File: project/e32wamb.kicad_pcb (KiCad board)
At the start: 2 copper layers, 50 x 37 mm, 31 parts, among them J1 2059-302_998-403, J2 Conn_01x04, J3 Conn_01x03, Q1 AO3400, Q2 AO3400, Q3 AO3400, Q4 AO3400, Q5 AO3400, SW1 TS-1187A-B-A-B, U1 AP63203WU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

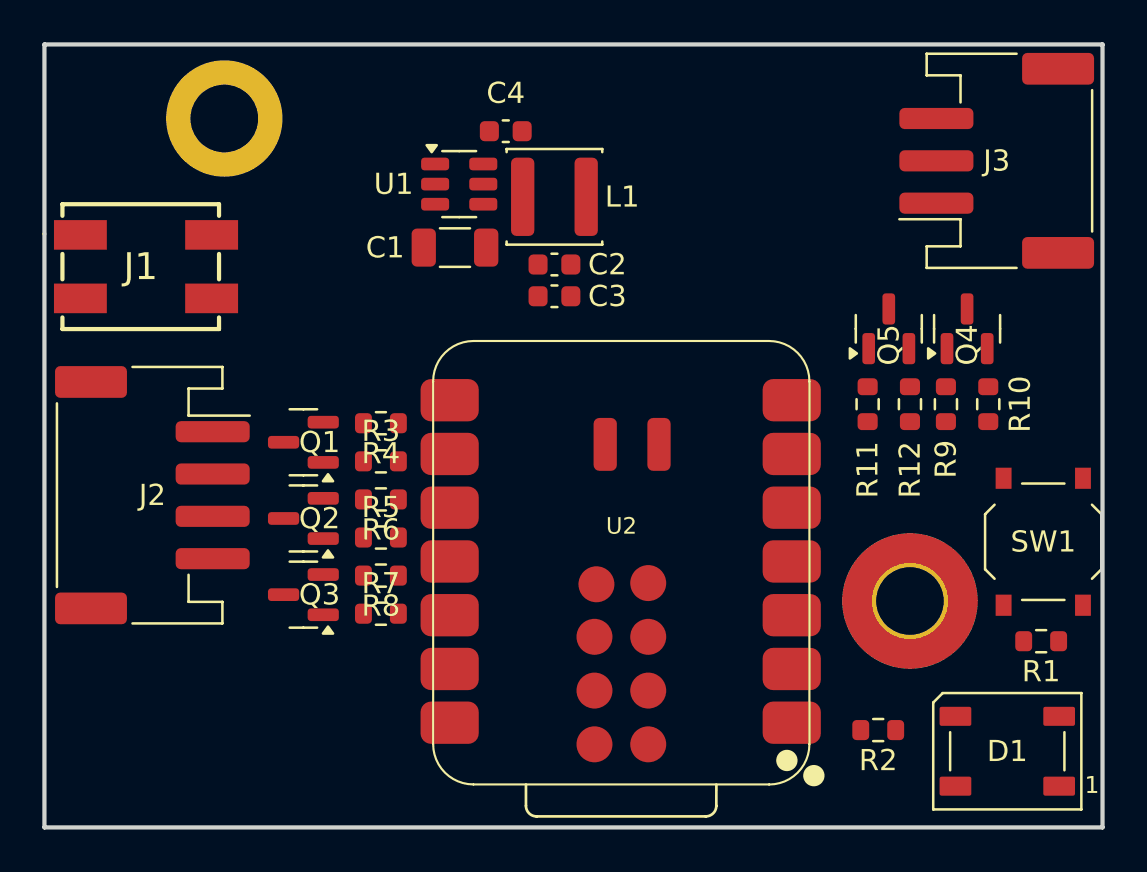
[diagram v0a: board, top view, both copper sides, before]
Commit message: First shot at wiring (complete pcb)
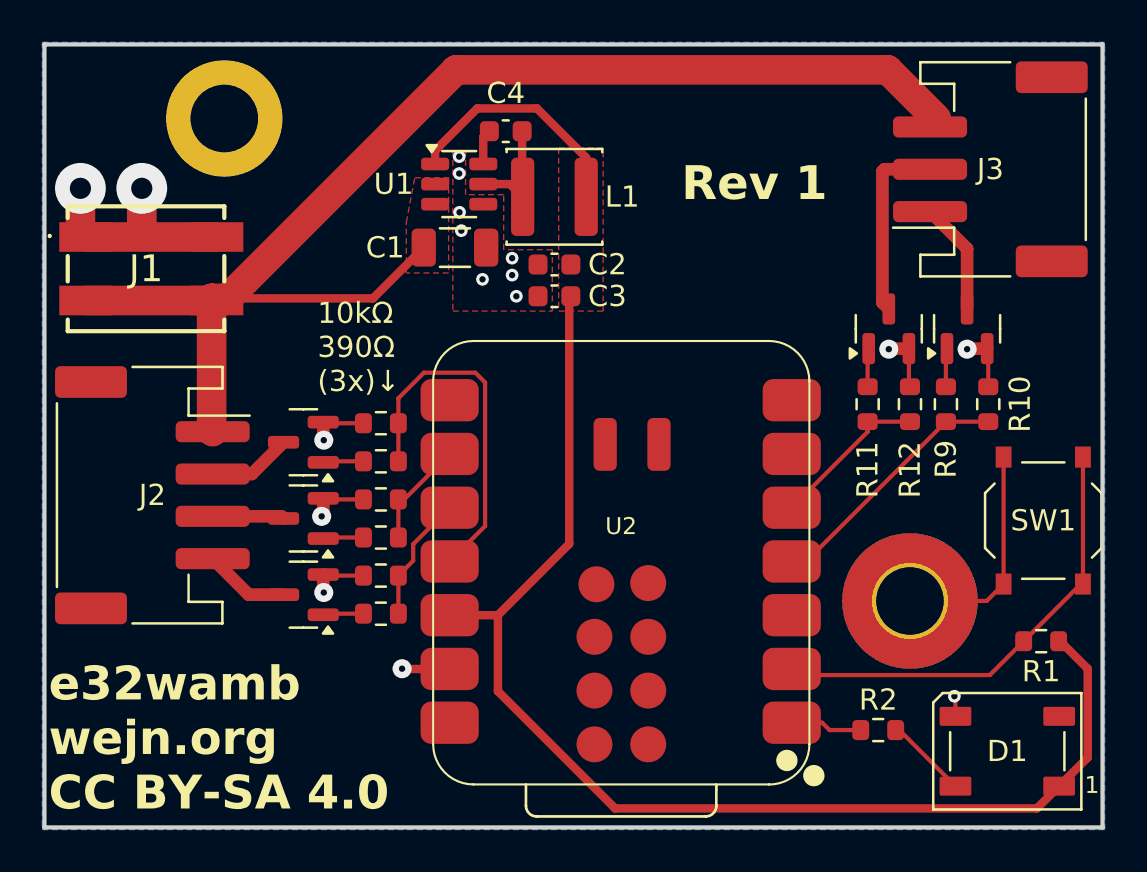
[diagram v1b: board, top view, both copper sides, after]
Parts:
- moved SW1 1.00 mm to (97.2, 72.5)
- moved J3 0.50 mm to (94.7, 55.9)
- moved J1 0.27 mm to (54.8, 60.6)
- turned R2 to 0 degrees
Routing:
- net +3.3V: track 0.00 -> 70.7 mm
- net VIN: track 0.00 -> 63.0 mm
- net GND: track 0.00 -> 39.2 mm, vias 0 -> 17
- net reset button: track 0.00 -> 21.7 mm
- net pwm drive 0: track 0.00 -> 16.9 mm
- net pwm drive 3: track 0.00 -> 12.0 mm
- net led 4: track 0.00 -> 8.92 mm
- net pwm drive 4: track 0.00 -> 7.55 mm
- net pwm drive 2: track 0.00 -> 6.01 mm
- net led 3: track 0.00 -> 5.32 mm
- net Net-(U1-SW): track 0.00 -> 5.22 mm
- net pwm drive 1: track 0.00 -> 5.11 mm
- net led 2: track 0.00 -> 4.05 mm
- net led 0: track 0.00 -> 3.97 mm
- net Net-(D1-DIN): track 0.00 -> 3.92 mm
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- added copper zone on F.Cu, net +3.3V
- added copper zone on B.Cu, net GND
- added copper zone on F.Cu, net GND
- added copper zone on F.Cu, net VIN
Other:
- board text added: "10kΩ 390Ω (3x)↓"
- board text added: "Rev 1"
- board text added: "e32wamb wejn.org CC BY-SA 4.0"

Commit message: Fix mounting hole h2 footprint
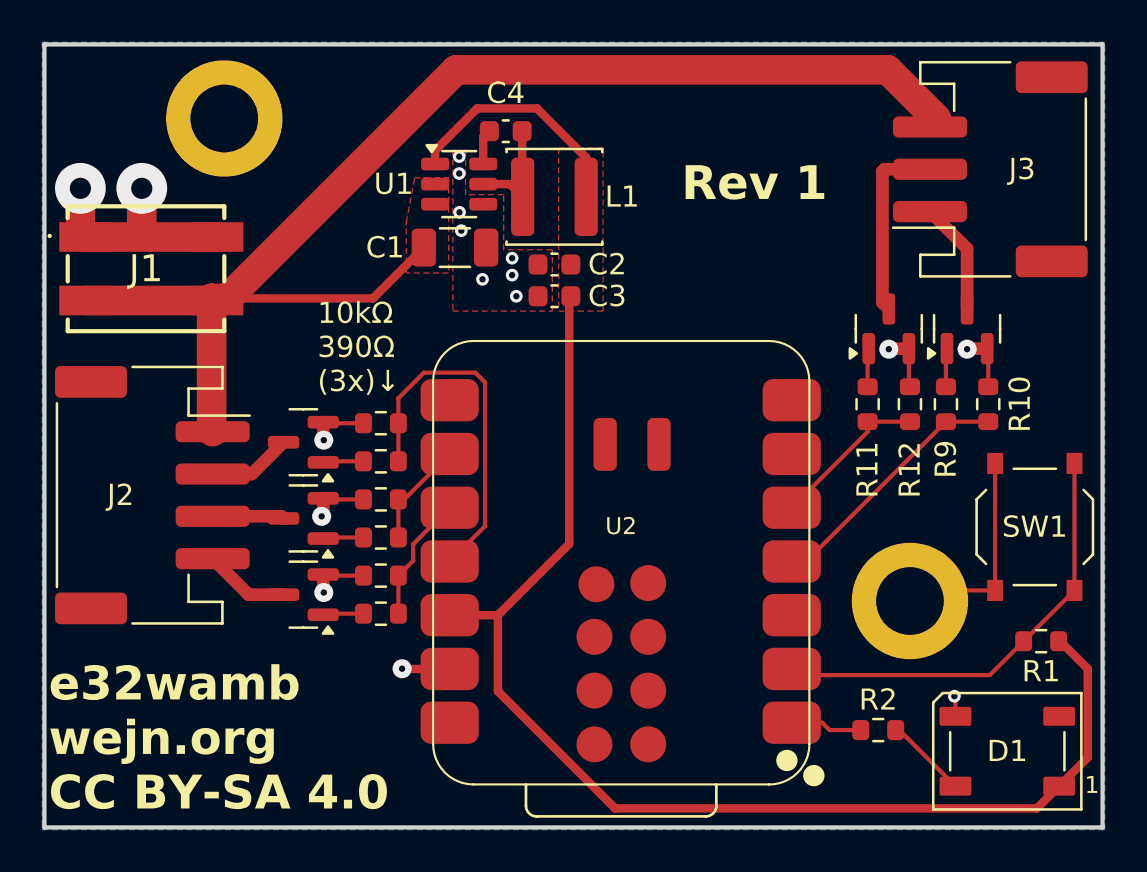
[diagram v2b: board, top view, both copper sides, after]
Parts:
- H2: footprint MountingHole:MountingHole_3.2mm_M3_Pad_TopBottom -> MountingHole:MountingHole_3.2mm_M3_ISO14580_Pad
- moved SW1 0.50 mm to (96.8, 72.8)
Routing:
- net reset button: track 21.7 -> 21.1 mm
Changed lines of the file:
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@@
 			(pdf_back_fp_property_popups yes)
 			(pdf_metadata yes)
-			(pdf_single_document no)
+			(pdf_single_document yes)
 			(dxfpolygonmode yes)
 			(dxfimperialunits yes)
@@
 			(psnegative no)
 			(psa4output no)
-			(plot_black_and_white yes)
+			(plot_black_and_white no)
 			(plotinvisibletext no)
 			(sketchpadsonfab no)
@@
 			(crossoutdnponfab yes)
 			(subtractmaskfromsilk no)
-			(outputformat 1)
+			(outputformat 4)
 			(mirror no)
-			(drillshape 1)
+			(drillshape 0)
 			(scaleselection 1)
-			(outputdirectory "")
+			(outputdirectory "/home/wejn/zz/")
 		)
 	)
@@
 		(tags "connector JST PH horizontal")
 		(property "Reference" "J2"
-			(at 0 0 0)
+			(at 0 1.5 0)
 			(layer "F.SilkS")
 			(effects
@@
 		)
 		(fp_text user "${REFERENCE}"
-			(at 0 1.5 90)
+			(at 0 1.5 180)
 			(layer "F.Fab")
 			(effects
@@
 		(tags "connector JST PH horizontal")
 		(property "Reference" "J3"
-			(at 0 0 180)
+			(at 0 1.5 180)
 			(layer "F.SilkS")
 			(effects
@@
 		)
 		(fp_text user "${REFERENCE}"
-			(at 0 1.5 90)
+			(at 0 1.5 180)
 			(layer "F.Fab")
 			(effects
@@
 		)
 	)
-	(footprint "MountingHole:MountingHole_3.2mm_M3_Pad_TopBottom"
+	(footprint "MountingHole:MountingHole_3.2mm_M3_ISO14580_Pad"
 		(layer "F.Cu")
 		(at 90.9 76.3)
-		(descr "Mounting Hole 3.2mm, M3")
-		(tags "mounting hole 3.2mm m3")
+		(descr "Mounting Hole 3.2mm, M3, ISO14580")
+		(tags "mounting hole 3.2mm m3 iso14580")
 		(property "Reference" "H2"
-			(at 0 -4.2 0)
+			(at 0 -3.75 0)
 			(layer "F.SilkS")
 			(hide yes)
@@
 		)
 		(property "Value" "MountingHole_Pad"
-			(at 0 4.2 0)
+			(at 0 3.75 0)
 			(layer "F.Fab")
 			(hide yes)
@@
 		(fp_circle
 			(center 0 0)
-			(end 3.2 0)
+			(end 2.75 0)
 			(stroke
 				(width 0.15)
@@
 		(fp_circle
 			(center 0 0)
-			(end 3.45 0)
+			(end 3 0)
 			(stroke
 				(width 0.05)
@@
 		(pad "1" thru_hole circle
 			(at 0 0)
-			(size 3.6 3.6)
+			(size 5.5 5.5)
 			(drill 3.2)
 			(layers "*.Cu" "*.Mask")
@@
 			(pintype "input")
 		)
-		(pad "1" connect circle
-			(at 0 0)
-			(size 6.4 6.4)
-			(layers "F.Cu" "F.Mask")
-			(net 2 "GND")
-			(pinfunction "1")
-			(pintype "input")
-		)
-		(pad "1" connect circle
-			(at 0 0)
-			(size 6.4 6.4)
-			(layers "B.Cu" "B.Mask")
-			(net 2 "GND")
-			(pinfunction "1")
-			(pintype "input")
-		)
 		(embedded_fonts no)
 	)
@@
 	(footprint "misc-lib:SW_Push_1P1T_XKB_TS-1187A"
 		(layer "F.Cu")
-		(at 97.2 72.5 -90)
+		(at 96.8 72.8 -90)
 		(descr "SMD Tactile Switch, http://www.helloxkb.com/public/images/pdf/TS-1187A-X-X-X.pdf")
 		(tags "SPST Tactile Switch")
@@
 	)
 	(segment
-		(start 90.9 76.3)
-		(end 94.525 76.3)
-		(width 0.2)
+		(start 63.175 71.45)
+		(end 63.175 72.225)
+		(width 0.6)
 		(layer "F.Cu")
 		(net 2)
 	)
 	(segment
-		(start 63.175 71.45)
-		(end 63.175 72.225)
-		(width 0.6)
+		(start 94.925 75.8)
+		(end 91.4 75.8)
+		(width 0.2)
 		(layer "F.Cu")
 		(net 2)
@@
 	)
 	(segment
+		(start 94.925 69.8)
+		(end 94.925 75.8)
+		(width 0.2)
+		(layer "F.Cu")
+		(net 2)
+	)
+	(segment
 		(start 51.95 59.1)
 		(end 58.15 59.1)
@@
 	)
 	(segment
-		(start 94.525 76.3)
-		(end 95.325 75.5)
-		(width 0.2)
+		(start 63.175 75.05)
+		(end 63.175 75.875)
+		(width 0.6)
 		(layer "F.Cu")
 		(net 2)
 	)
 	(segment
-		(start 63.175 75.05)
-		(end 63.175 75.875)
-		(width 0.6)
+		(start 91.4 75.8)
+		(end 90.9 76.3)
+		(width 0.2)
 		(layer "F.Cu")
 		(net 2)
@@
 	)
 	(segment
-		(start 95.325 69.5)
-		(end 95.325 75.5)
-		(width 0.2)
-		(layer "F.Cu")
-		(net 2)
-	)
-	(segment
 		(start 69.6 55.2)
 		(end 69.614574 55.214574)
@@
 	)
 	(segment
+		(start 94.925 69.8)
+		(end 94.9 69.8)
+		(width 0.6)
+		(layer "F.Cu")
+		(net 2)
+	)
+	(segment
 		(start 63.175 75.875)
 		(end 63.2 75.9)
@@
 	)
 	(segment
-		(start 99.075 75.5)
-		(end 98.975 75.5)
+		(start 98.675 69.8)
+		(end 98.675 75.8)
 		(width 0.2)
 		(layer "F.Cu")
@@
 	)
 	(segment
-		(start 99.075 69.5)
-		(end 99.075 75.5)
-		(width 0.2)
-		(layer "F.Cu")
-		(net 18)
-	)
-	(segment
-		(start 98.975 75.5)
-		(end 96.275 78.2)
+		(start 96.275 78.2)
+		(end 98.675 75.8)
 		(width 0.2)
 		(layer "F.Cu")

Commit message: Add jlcpcb tooling holes
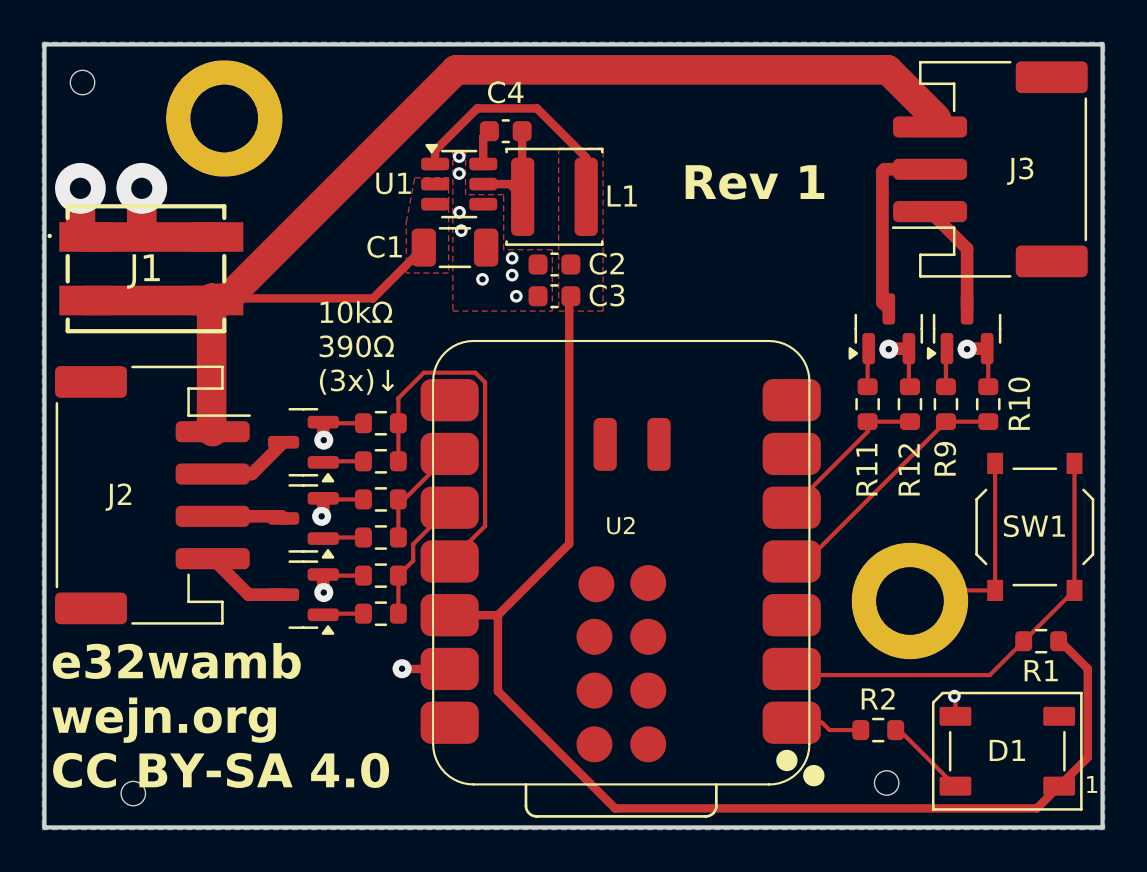
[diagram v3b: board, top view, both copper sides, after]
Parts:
- added REF**: ToolingHole_1.152mm, MountingHole:ToolingHole_1.152mm, F.Cu at (51.8, 51.8)
- added REF**: ToolingHole_1.152mm, MountingHole:ToolingHole_1.152mm, F.Cu at (54.2, 85.4)
- added REF**: ToolingHole_1.152mm, MountingHole:ToolingHole_1.152mm, F.Cu at (89.8, 84.9)
